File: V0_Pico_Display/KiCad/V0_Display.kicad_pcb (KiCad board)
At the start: 2 copper layers, 80 x 35 mm, 17 parts, among them J2 I2C Header 1, J7 USB_Header, J8 Conn_01x02, SW5 SW_SPST, SW6 SW_SPST, SW7 Rotary_Encoder_Switch, U1 Pico, U3 74LVC1G17

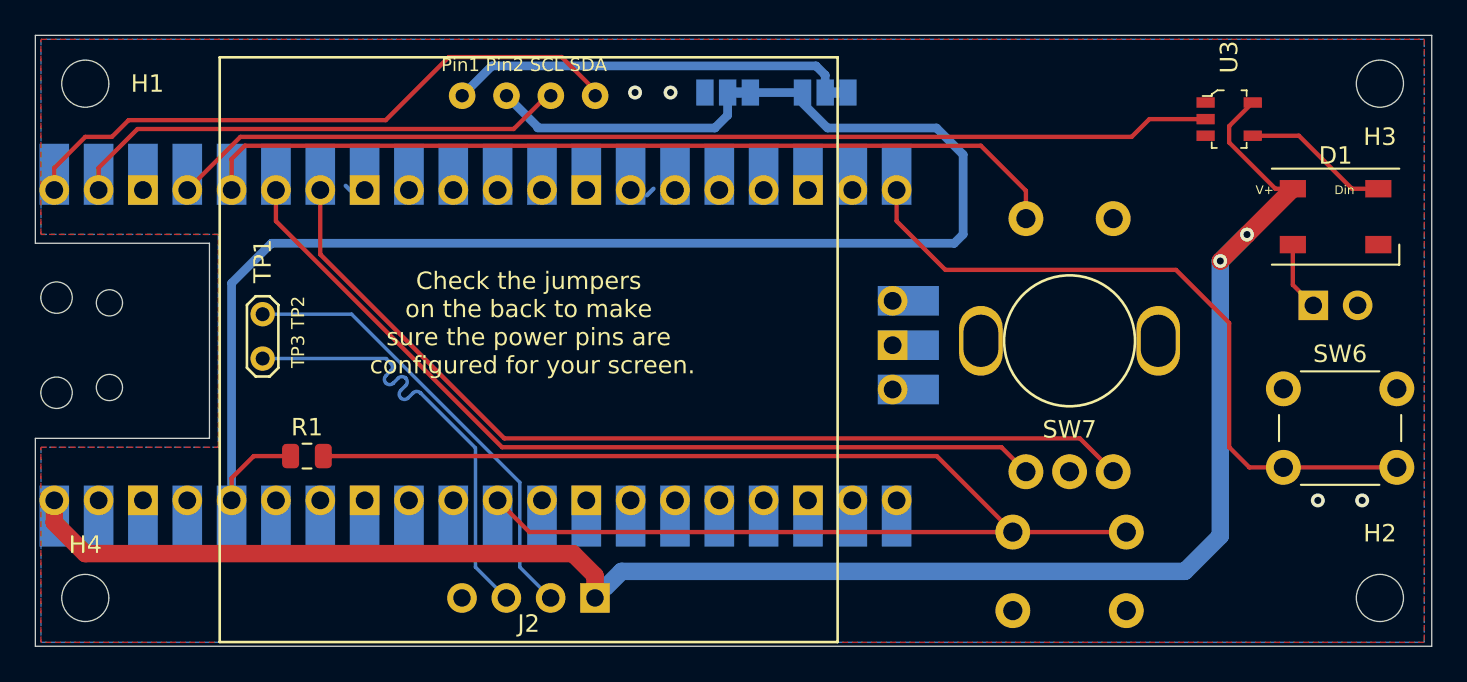
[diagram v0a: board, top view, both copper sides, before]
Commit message: flip TP2 TP3 pin to prevent cross-wired
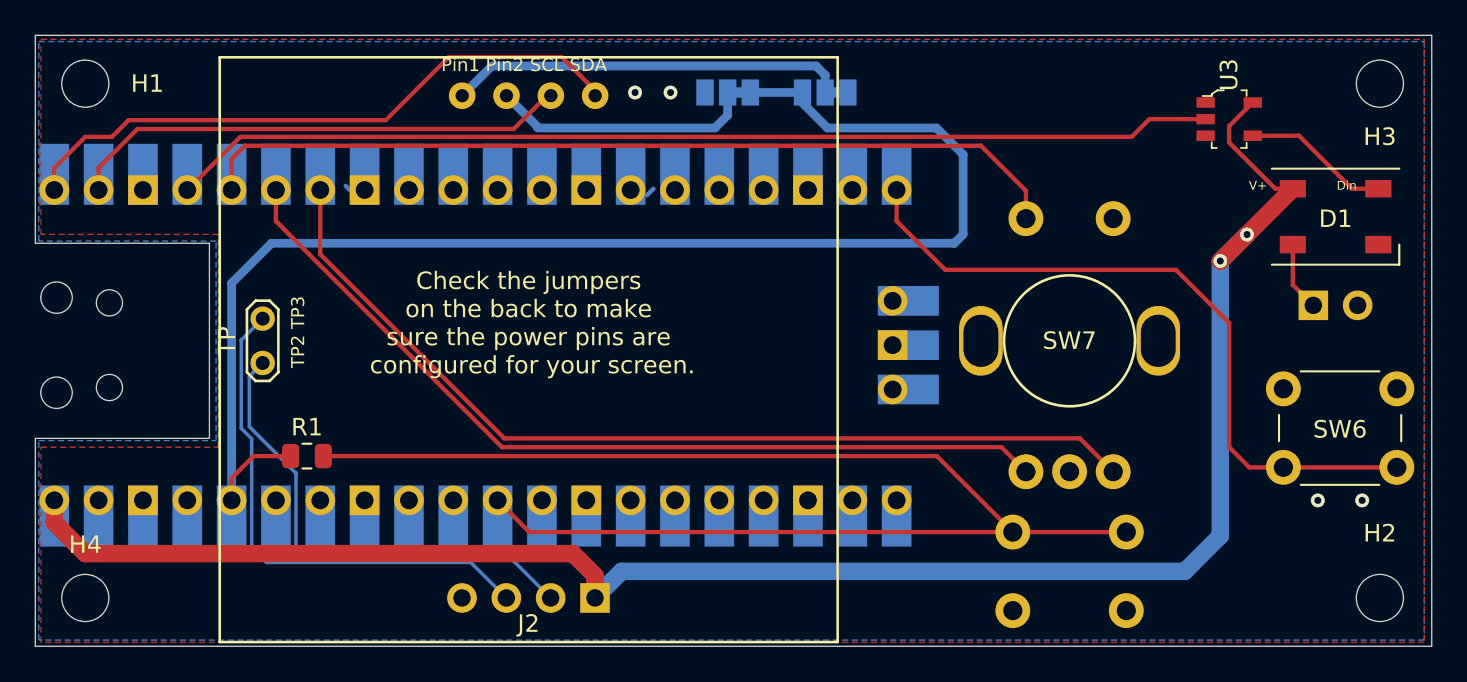
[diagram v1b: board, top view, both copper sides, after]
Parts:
- moved TP 2.79 mm to (98.2, 68.4), turned to 90 degrees
- renumbered TP1 to TP
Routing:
- net D+: track 26.5 -> 29.7 mm
- net D-: track 26.1 -> 27.8 mm
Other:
- board text added: "Gnd D-Out"
- board text added: "TP2 TP3"
- board text removed: "Gnd Neo-Out"
- board text removed: "TP3 TP2"
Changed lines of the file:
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@@
     (property "Sheetname" "")
     (attr through_hole)
-    (fp_text reference "SW6" (at 3.25 -2) (layer "F.SilkS")
+    (fp_text reference "SW6" (at 3.25 2.33) (layer "F.SilkS")
       (effects (font (size 1 1) (thickness 0.15)))
     )
@@
     (property "Sheetname" "")
     (attr through_hole)
-    (fp_text reference "SW7" (at 0 5.08) (layer "F.SilkS")
+    (fp_text reference "SW7" (at 0 0) (layer "F.SilkS")
       (effects (font (size 1 1) (thickness 0.15)))
     )
@@
     (property "Sheetname" "")
     (attr smd)
-    (fp_text reference "D1" (at 0 -3.5) (layer "F.SilkS")
+    (fp_text reference "D1" (at 0 0.127) (layer "F.SilkS")
       (effects (font (size 1 1) (thickness 0.15)))
     )
@@
   )
   (footprint "TestPoint:TestPoint_2Pads_Pitch2.54mm_Drill0.8mm" (layer "F.Cu")
-    (at 98.192 65.626 -90)
+    (at 98.192 68.42 90)
     (descr "Test point with 2 pins, pitch 2.54mm, drill diameter 0.8mm")
     (tags "CONN DEV")
@@
     (property "Sheetname" "")
     (attr exclude_from_pos_files)
-    (fp_text reference "TP1" (at -3.048 0 90) (layer "F.SilkS")
+    (fp_text reference "TP" (at 1.27 -2.032 90) (layer "F.SilkS")
       (effects (font (size 1 1) (thickness 0.15)))
     )
@@
     (fp_line (start -1.3 -0.5) (end -1.3 0.5) (layer "F.CrtYd") (width 0.05))
     (fp_line (start 3.15 1.15) (end 3.8 0.5) (layer "F.CrtYd") (width 0.05))
-    (pad "1" thru_hole circle (at 0 0 270) (size 1.4 1.4) (drill 0.8) (layers *.Cu *.Mask)
+    (pad "1" thru_hole circle (at 0 0 90) (size 1.4 1.4) (drill 0.8) (layers *.Cu *.Mask)
       (net 5 "D-") (pinfunction "1") (pintype "passive"))
-    (pad "2" thru_hole circle (at 2.54 0 270) (size 1.4 1.4) (drill 0.8) (layers *.Cu *.Mask)
+    (pad "2" thru_hole circle (at 2.54 0 90) (size 1.4 1.4) (drill 0.8) (layers *.Cu *.Mask)
       (net 4 "D+") (pinfunction "2") (pintype "passive"))
   )
@@
     (property "Sheetname" "")
     (attr smd)
-    (fp_text reference "U3" (at -3.556 0 90) (layer "F.SilkS")
+    (fp_text reference "U3" (at -2.54 0 90) (layer "F.SilkS")
       (effects (font (size 1 1) (thickness 0.15)))
     )
@@
     (property "Sheetname" "")
     (attr through_hole)
-    (fp_text reference "SW5" (at 3.25 2) (layer "B.SilkS")
+    (fp_text reference "SW5" (at 3.25 -2.377) (layer "B.SilkS")
       (effects (font (size 1 1) (thickness 0.15)) (justify mirror))
     )
@@
     (effects (font (size 1.5 1.5) (thickness 0.2)) (justify mirror))
   )
-  (gr_text "Gnd Neo-Out" (at 159.152 62.578) (layer "B.SilkS")
+  (gr_text "Gnd D-Out" (at 159.66 62.705) (layer "B.SilkS")
     (effects (font (size 0.5 0.5) (thickness 0.1)) (justify mirror))
   )
@@
     (effects (font (size 0.75 0.75) (thickness 0.1)) (justify mirror))
   )
-  (gr_text "V+" (at 155.596 58.514) (layer "F.SilkS")
+  (gr_text "V+" (at 155.215 58.26) (layer "F.SilkS")
     (effects (font (size 0.5 0.5) (thickness 0.075)))
   )
@@
     (effects (font (size 0.75 0.75) (thickness 0.1)))
   )
-  (gr_text "TP3 TP2" (at 100.224 66.642 90) (layer "F.SilkS")
+  (gr_text "TP2 TP3" (at 100.224 66.642 90) (layer "F.SilkS")
     (effects (font (size 0.75 0.75) (thickness 0.1)))
   )
-  (gr_text "Din" (at 160.168 58.514) (layer "F.SilkS")
+  (gr_text "Din" (at 160.295 58.26) (layer "F.SilkS")
     (effects (font (size 0.5 0.5) (thickness 0.075)))
   )
@@
   (segment (start 138.324 61.054) (end 138.324 56.482) (width 0.5) (layer "B.Cu") (net 3))
   (segment (start 129.12 53.525022) (end 129.12 52.926) (width 0.25) (layer "B.Cu") (net 3))
-  (segment (start 105.538007 68.864257) (end 105.538008 68.864256) (width 0.2) (layer "B.Cu") (net 4))
-  (segment (start 106.386536 69.712784) (end 106.103693 69.995626) (width 0.2) (layer "B.Cu") (net 4))
-  (segment (start 106.386535 69.712785) (end 106.386536 69.712784) (width 0.2) (layer "B.Cu") (net 4))
-  (segment (start 106.527957 70.41989) (end 106.810799 70.137047) (width 0.2) (layer "B.Cu") (net 4))
-  (segment (start 110.384 73.285984) (end 110.384 80.114) (width 0.2) (layer "B.Cu") (net 4))
-  (segment (start 106.386535 69.288519) (end 106.386536 69.28852) (width 0.2) (layer "B.Cu") (net 4))
-  (segment (start 98.192 68.166) (end 105.264016 68.166) (width 0.2) (layer "B.Cu") (net 4))
-  (segment (start 105.67943 69.571361) (end 105.679429 69.571362) (width 0.2) (layer "B.Cu") (net 4))
-  (segment (start 105.264016 68.166) (end 105.538008 68.439992) (width 0.2) (layer "B.Cu") (net 4))
-  (segment (start 107.235063 70.137047) (end 107.235064 70.137048) (width 0.2) (layer "B.Cu") (net 4))
-  (segment (start 107.235064 70.137048) (end 110.384 73.285984) (width 0.2) (layer "B.Cu") (net 4))
-  (segment (start 110.384 80.114) (end 112.152 81.882) (width 0.2) (layer "B.Cu") (net 4))
-  (segment (start 105.679429 69.571362) (end 105.962271 69.288519) (width 0.2) (layer "B.Cu") (net 4))
-  (segment (start 105.538008 68.864256) (end 105.255165 69.147098) (width 0.2) (layer "B.Cu") (net 4))
-  (segment (start 106.527958 70.419889) (end 106.527957 70.41989) (width 0.2) (layer "B.Cu") (net 4))
-  (arc (start 106.103693 70.41989) (mid 106.315826 70.507758) (end 106.527958 70.419889) (width 0.2) (layer "B.Cu") (net 4))
-  (arc (start 106.103693 69.995626) (mid 106.015825 70.207758) (end 106.103693 70.41989) (width 0.2) (layer "B.Cu") (net 4))
-  (arc (start 106.386536 69.28852) (mid 106.474404 69.500653) (end 106.386535 69.712785) (width 0.2) (layer "B.Cu") (net 4))
-  (arc (start 106.810799 70.137047) (mid 107.022931 70.049179) (end 107.235063 70.137047) (width 0.2) (layer "B.Cu") (net 4))
-  (arc (start 105.255165 69.147098) (mid 105.167297 69.35923) (end 105.255165 69.571362) (width 0.2) (layer "B.Cu") (net 4))
-  (arc (start 105.538008 68.439992) (mid 105.625876 68.652125) (end 105.538007 68.864257) (width 0.2) (layer "B.Cu") (net 4))
-  (arc (start 105.962271 69.288519) (mid 106.174403 69.200651) (end 106.386535 69.288519) (width 0.2) (layer "B.Cu") (net 4))
-  (arc (start 105.255165 69.571362) (mid 105.467298 69.65923) (end 105.67943 69.571361) (width 0.2) (layer "B.Cu") (net 4))
-  (segment (start 98.192 65.626) (end 103.289022 65.626) (width 0.2) (layer "B.Cu") (net 5))
-  (segment (start 103.289022 65.626) (end 112.924 75.260978) (width 0.2) (layer "B.Cu") (net 5))
-  (segment (start 112.924 75.260978) (end 112.924 80.114) (width 0.2) (layer "B.Cu") (net 5))
-  (segment (start 112.924 80.114) (end 114.692 81.882) (width 0.2) (layer "B.Cu") (net 5))
+  (segment (start 110.12 79.85) (end 112.152 81.882) (width 0.2) (layer "B.Cu") (net 4))
+  (segment (start 96.96352 67.10848) (end 96.96352 72.164512) (width 0.2) (layer "B.Cu") (net 4))
+  (segment (start 97.563511 78.998533) (end 98.414978 79.85) (width 0.2) (layer "B.Cu") (net 4))
+  (segment (start 97.563511 72.764503) (end 97.563511 78.998533) (width 0.2) (layer "B.Cu") (net 4))
+  (segment (start 98.414978 79.85) (end 110.12 79.85) (width 0.2) (layer "B.Cu") (net 4))
+  (segment (start 98.192 65.88) (end 96.96352 67.10848) (width 0.2) (layer "B.Cu") (net 4))
+  (segment (start 96.96352 72.164512) (end 97.563511 72.764503) (width 0.2) (layer "B.Cu") (net 4))
+  (segment (start 100.344489 79.239511) (end 112.049511 79.239511) (width 0.2) (layer "B.Cu") (net 5))
+  (segment (start 112.049511 79.239511) (end 114.692 81.882) (width 0.2) (layer "B.Cu") (net 5))
+  (segment (start 100.103511 78.998533) (end 100.344489 79.239511) (width 0.2) (layer "B.Cu") (net 5))
+  (segment (start 97.43 69.182) (end 97.43 72.065986) (width 0.2) (layer "B.Cu") (net 5))
+  (segment (start 100.103511 74.739497) (end 100.103511 78.998533) (width 0.2) (layer "B.Cu") (net 5))
+  (segment (start 98.192 68.42) (end 97.43 69.182) (width 0.2) (layer "B.Cu") (net 5))
+  (segment (start 97.43 72.065986) (end 100.103511 74.739497) (width 0.2) (layer "B.Cu") (net 5))
   (segment (start 115.324 50.894) (end 117.28 52.85) (width 0.25) (layer "F.Cu") (net 6))
   (segment (start 90.51352 54.50848) (end 105.24552 54.50848) (width 0.25) (layer "F.Cu") (net 6))
@@
     (connect_pads (clearance 0.508))
     (min_thickness 0.254) (filled_areas_thickness no)
-    (fill yes (thermal_gap 0.508) (thermal_bridge_width 0.508))
+    (fill yes (thermal_gap 0.508) (thermal_bridge_width 0.508) (island_removal_mode 1) (island_area_min 0))
     (polygon
       (pts
@@
     (connect_pads (clearance 0.508))
     (min_thickness 0.254) (filled_areas_thickness no)
-    (fill yes (thermal_gap 0.508) (thermal_bridge_width 0.508))
+    (fill yes (thermal_gap 0.508) (thermal_bridge_width 0.508) (island_removal_mode 1) (island_area_min 0))
     (polygon
       (pts
-        (xy 164.74 49.878)
-        (xy 85.492 49.878)
-        (xy 85.492 61.054)
-        (xy 95.652 61.054)
-        (xy 95.652 73.246)
-        (xy 85.492 73.246)
-        (xy 85.492 84.422)
-        (xy 164.74 84.422)
+        (xy 164.74 84.295)
+        (xy 85.365 84.295)
+        (xy 85.365 72.865)
+        (xy 95.525 72.865)
+        (xy 95.525 61.435)
+        (xy 85.365 61.435)
+        (xy 85.365 50.005)
+        (xy 164.74 50.005)
       )
     )
